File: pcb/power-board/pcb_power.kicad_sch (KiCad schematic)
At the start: 3 parts, among them J10 JST_B4B-XH-A, J11 JST_B4P-VH, J12 XT30

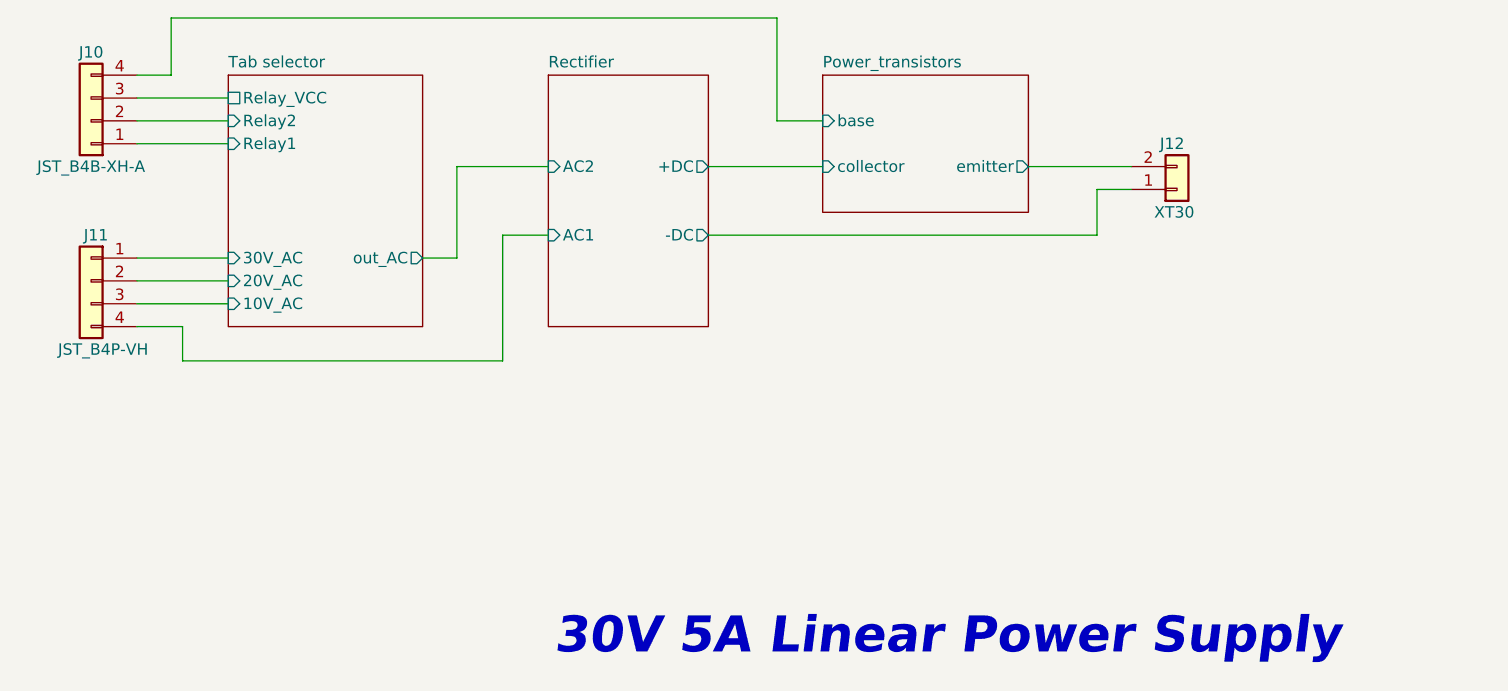
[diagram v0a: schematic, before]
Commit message: Perform minor stylistic changes on power-board schematic, clear DRC
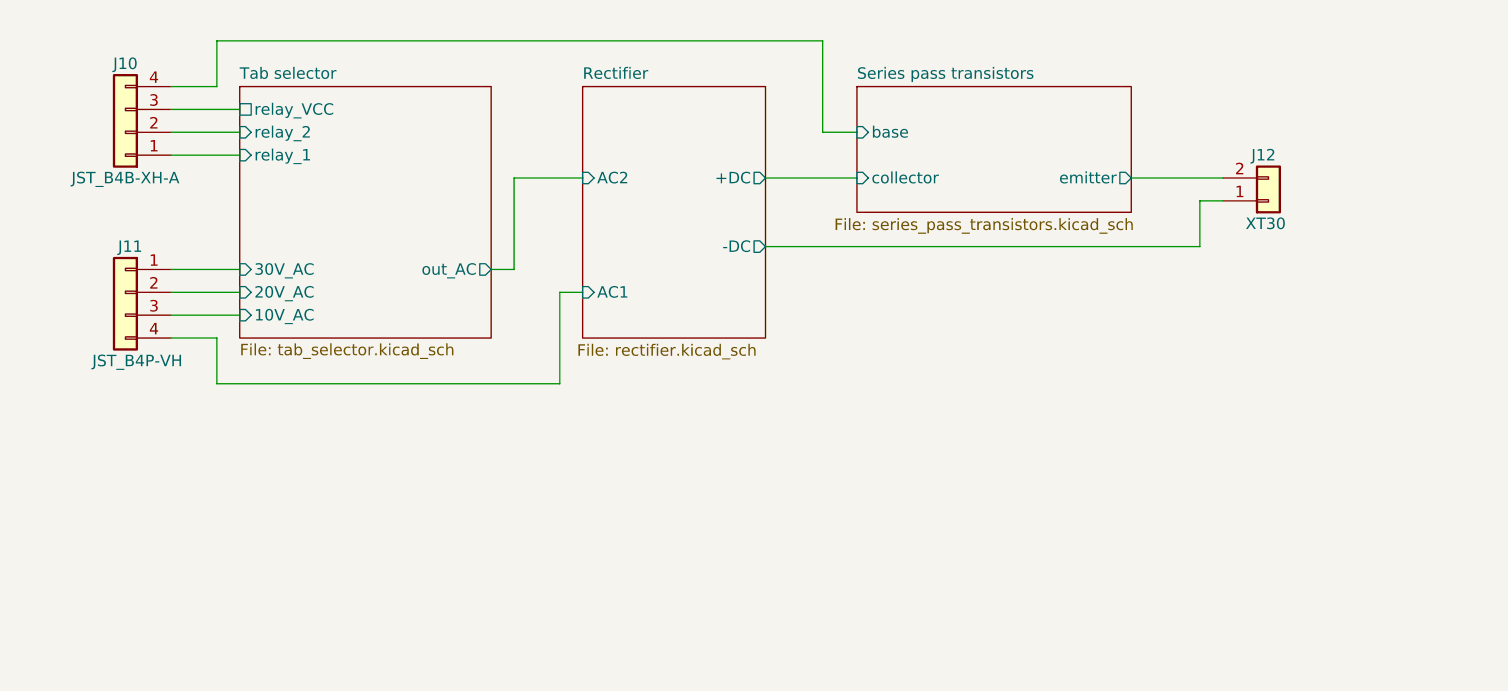
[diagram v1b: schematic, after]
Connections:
- net Tab selector/Relay1 renamed Tab selector/relay_1
- net Tab selector/Relay2 renamed Tab selector/relay_2
- net Tab selector/Relay_VCC renamed Tab selector/relay_VCC
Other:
- sheet Power_transistors renamed Series pass transistors
- sheet Series pass transistors: file power_transistors.kicad_sch -> series_pass_transistors.kicad_sch
- sheet Tab selector ports: added relay_1, relay_2, relay_VCC; removed Relay1, Relay2, Relay_VCC
- note removed: "30V 5A Linear Power Supply"
- title: Tab selector, rectifier, series pass transistors -> DW3005T-power-board
- moved on the sheet: J10, J11, J12
